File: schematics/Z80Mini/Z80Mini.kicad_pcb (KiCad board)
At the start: 2 copper layers, 194.3 x 105.4 mm, 65 parts, among them J1 Conn_02x20_Odd_Even, J2 TTL Serial, J3 USB_B_Micro, J4 Conn_02x10_Counter_Clockwise, Q1 BC337, Q2 IRLML6402, SW1 RESET, SW2 SW_DIP_x04, U1 CPU Z80, U2 SRAM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

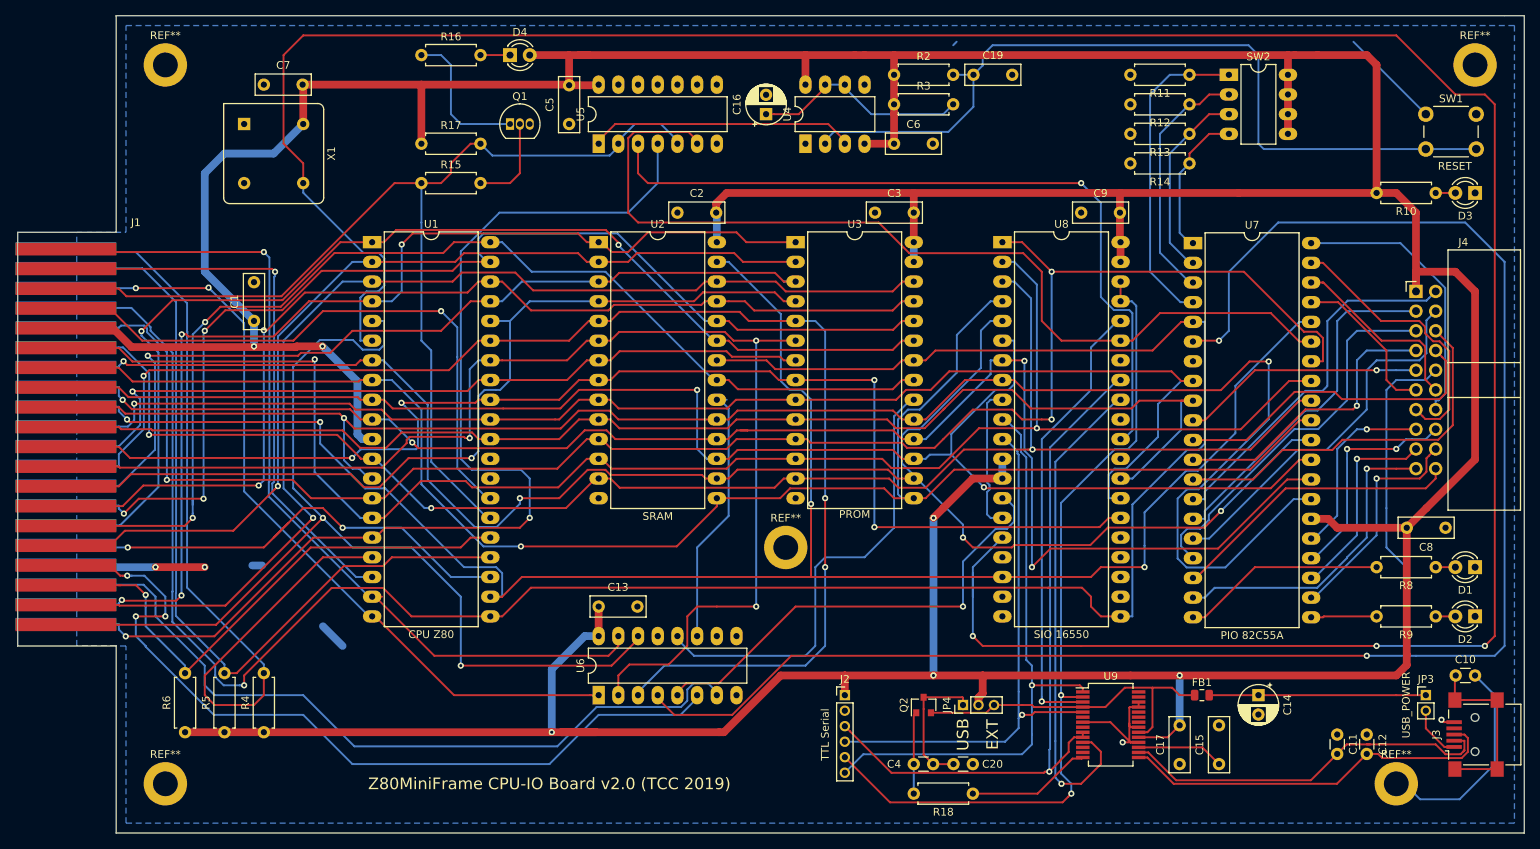
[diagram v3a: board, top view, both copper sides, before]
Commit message: Latest changes on vdp routines and bas32k added new COLOR instruction
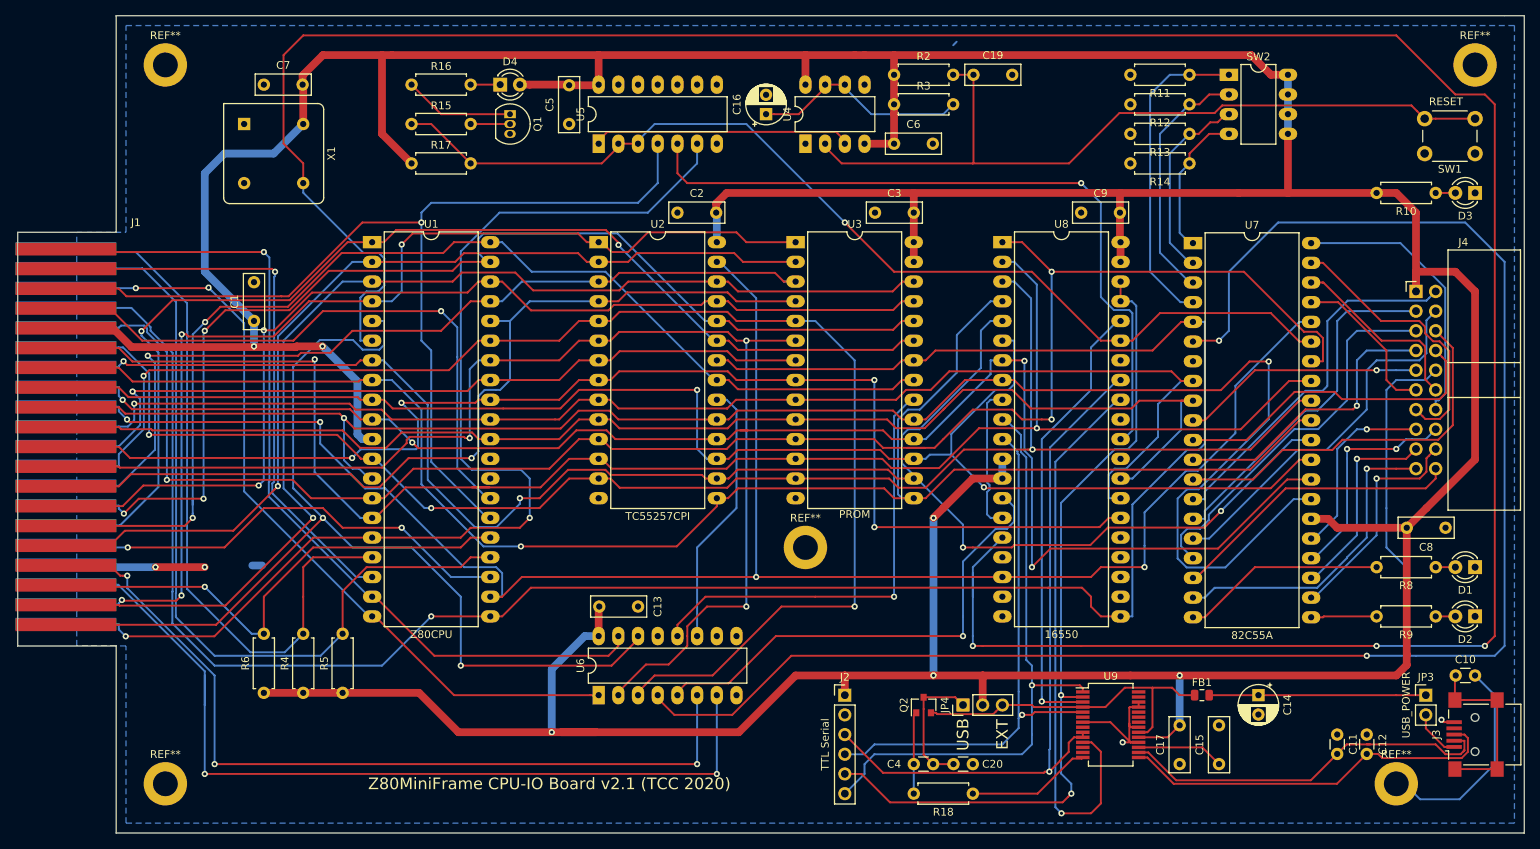
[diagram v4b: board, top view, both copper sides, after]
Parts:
- J2: footprint Connector_PinHeader_2.00mm:PinHeader_1x06_P2.00mm_Vertical -> Connector_PinHeader_2.54mm:PinHeader_1x06_P2.54mm_Vertical
- JP3: footprint Connector_PinHeader_2.00mm:PinHeader_1x02_P2.00mm_Vertical -> Connector_PinHeader_2.54mm:PinHeader_1x02_P2.54mm_Vertical
- JP4: footprint Connector_PinHeader_2.00mm:PinHeader_1x03_P2.00mm_Vertical -> Connector_PinHeader_2.54mm:PinHeader_1x03_P2.54mm_Vertical
- U1: value CPU Z80 -> Z80CPU
- U2: value SRAM -> TC55257CPI
- U7: value PIO 82C55A -> 82C55A
- U8: value SIO 16550 -> 16550
- moved R5 16.1 mm to (106.7, 131.8)
- moved R6 11.4 mm to (96.5, 131.8)
- moved SW1 8.13 mm to (252.7, 62.2), turned to 180 degrees
- moved R15 7.73 mm to (115.6, 58.4)
- moved R4 7.18 mm to (101.6, 131.8)
- moved C13 5.08 mm to (144.8, 120.7), turned to 180 degrees
- moved D4 4.02 mm to (127.0, 53.3)
- moved R16 4.02 mm to (115.6, 53.3)
- moved R17 2.84 mm to (115.6, 63.5)
- moved REF** 2.54 mm to (166.4, 113.0)
- moved Q1 1.27 mm to (128.3, 57.1), turned to 270 degrees
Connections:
- C13 pad 1: +5V -> GND
- C13 pad 2: GND -> +5V
- R15 pad 1: /RESET -> IO_RESET
- R17 pad 2: /RESET -> IO_RESET
- U5 pad 2: /RESET -> IO_RESET
- U5 pad 3: /IO_UART/UART_INTR -> IO_RESET
- U5 pad 4: /INT -> /RESET
- U5 pad 5: /RESET -> /IO_UART/UART_INTR
- U5 pad 6: IO_RESET -> /INT
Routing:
- net +5V: track 768.2 -> 748.1 mm
- net NMI: track 112.5 -> 93.0 mm
- net GND: track 120.3 -> 103.5 mm
- net /SND_SEL: track 100.6 -> 115.8 mm, vias 0 -> 2
- net IO_RESET: track 121.3 -> 135.3 mm, vias 0 -> 1
- net /RESET: track 139.3 -> 130.6 mm, vias 0 -> 1
- net Net-(U8-Pad32): track 64.1 -> 72.5 mm
- net RD: track 299.4 -> 292.5 mm
- net Net-(Q1-Pad2): track 12.0 -> 5.08 mm
- net /IO_UART/UART_INTR: track 99.7 -> 94.2 mm
- net Net-(C19-Pad1): track 107.5 -> 102.6 mm
- net /BUSRQ: track 69.9 -> 65.3 mm
- net Net-(Q1-Pad1): track 18.8 -> 14.3 mm
- net WR: track 248.9 -> 244.4 mm
- net /INT: track 143.5 -> 147.1 mm
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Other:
- board text added: "Z80MiniFrame CPU-IO Board v2.1 (TCC 2020)"
- board text removed: "Z80MiniFrame CPU-IO Board v2.0 (TCC 2019)"

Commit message: Created new schematic for TTLSerial to USB, I2C and RS232
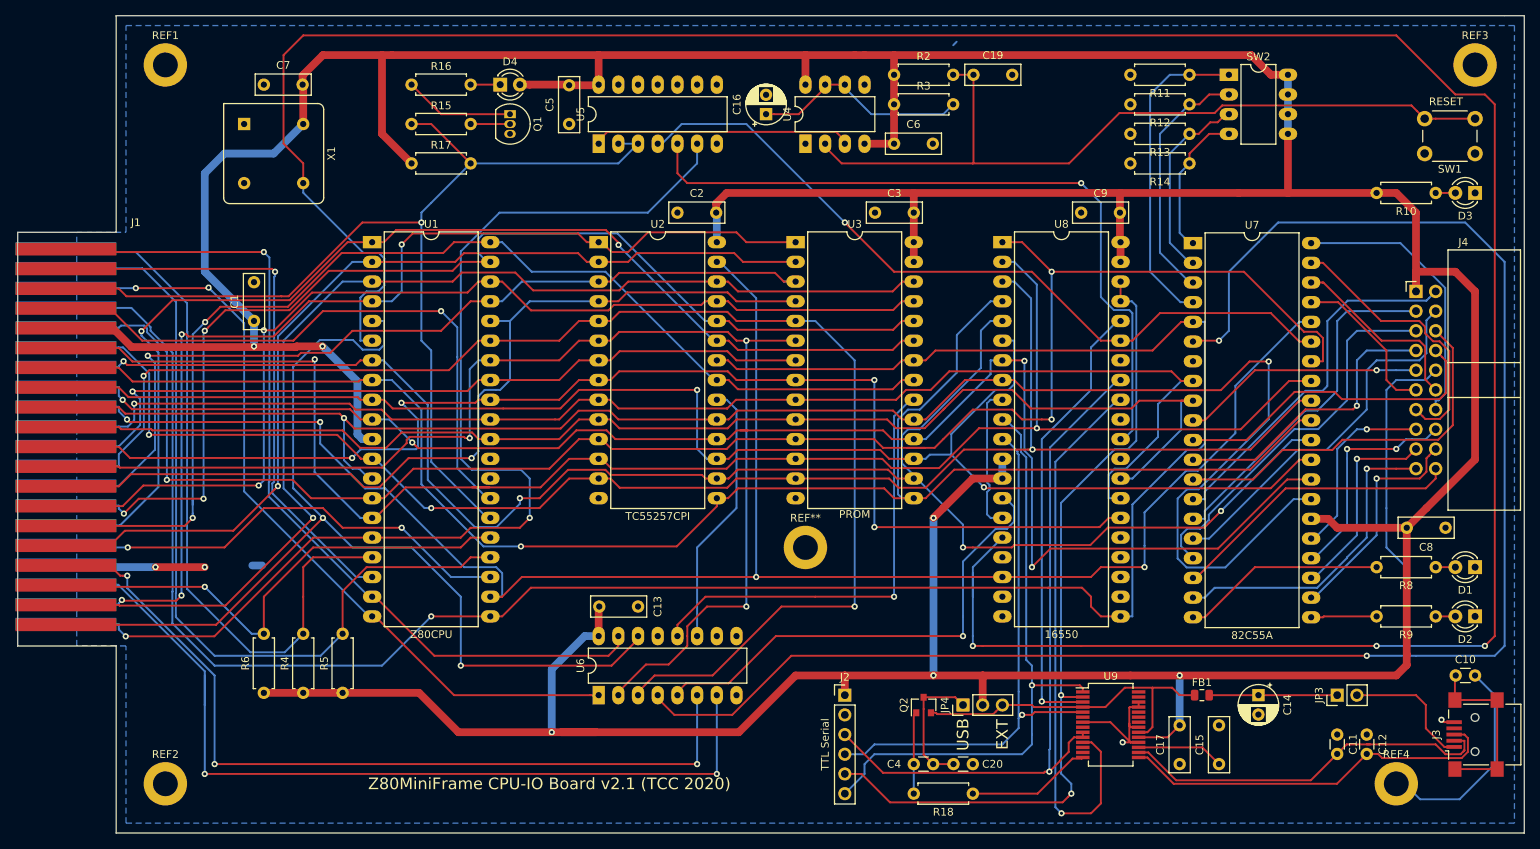
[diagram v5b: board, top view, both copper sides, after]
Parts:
- JP3: value USB_POWER -> USB_VBUS
- moved JP3 11.4 mm to (234.9, 132.1), turned to 90 degrees
- renumbered REF** to REF1, REF** to REF2, REF** to REF3, REF** to REF4
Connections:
- R15 pad 1: IO_RESET -> /RESET
- R17 pad 2: IO_RESET -> /RESET
- U5 pad 2: IO_RESET -> /RESET
- U5 pad 3: IO_RESET -> /RESET
- U5 pad 4: /RESET -> IO_RESET
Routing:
- net IO_RESET: track 135.3 -> 99.9 mm
- net Net-(C14-Pad1): track 27.9 -> 16.5 mm
- net Net-(J3-Pad1): track 6.92 -> 17.1 mm
- net /RESET: track 130.6 -> 137.4 mm
